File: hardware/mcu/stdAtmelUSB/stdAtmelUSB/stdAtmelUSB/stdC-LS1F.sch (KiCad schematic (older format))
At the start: 1 part

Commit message: std boards skeletons
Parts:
- added C2: 4.7uF, Capacitor_SMD:C_0402_1005Metric, symbol Device:C
- added C4: 0.1uF, Capacitor_SMD:C_0402_1005Metric, symbol Device:C
- J1: renamed from J?; footprint (none) -> Connector_PinHeader_2.54mm:PinHeader_1x20_P2.54mm_Horizontal
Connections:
- net labels added: fpga_cdone, fpga_reset, nrf_rx, nrf_tx, spi_clk, spi_miso, spi_mosi, spi_ss, uart_fpga_rx_2, uart_fpga_tx_2, uart_rx, uart_tx
- wire segments 2 -> 24
- no-connect marks 0 -> 1
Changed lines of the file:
@@
 $EndDescr
 $Comp
-L Connector:Conn_01x20_Female J?
+L Connector:Conn_01x20_Female J1
 U 1 1 5E9E9075
 P 2050 3500
-F 0 "J?" H 1942 2275 50  0000 C CNN
+F 0 "J1" H 1942 2275 50  0000 C CNN
 F 1 "Conn_01x20_Female" H 1942 2366 50  0000 C CNN
-F 2 "" H 2050 3500 50  0001 C CNN
+F 2 "Connector_PinHeader_2.54mm:PinHeader_1x20_P2.54mm_Horizontal" H 2050 3500 50  0001 C CNN
 F 3 "~" H 2050 3500 50  0001 C CNN
 	1    2050 3500
@@
 P 3350 1800
 AR Path="/5E9E6BE4/5E9ECCA0" Ref="#PWR?"  Part="1"
-AR Path="/5E9E8D09/5E9ECCA0" Ref="#PWR?"  Part="1"
-F 0 "#PWR?" H 3350 1650 50  0001 C CNN
+AR Path="/5E9E8D09/5E9ECCA0" Ref="#PWR04"  Part="1"
+F 0 "#PWR04" H 3350 1650 50  0001 C CNN
 F 1 "+3V3" H 3365 1973 50  0000 C CNN
 F 2 "" H 3350 1800 50  0001 C CNN
@@
 	1    0    0    -1
 $EndComp
-Wire Wire Line
-	3350 1800 3350 2050
 $Comp
-L power:GND #PWR?
+L power:GND #PWR03
 U 1 1 5E9EE351
 P 3000 4900
-F 0 "#PWR?" H 3000 4650 50  0001 C CNN
+F 0 "#PWR03" H 3000 4650 50  0001 C CNN
 F 1 "GND" H 3005 4727 50  0000 C CNN
 F 2 "" H 3000 4900 50  0001 C CNN
@@
 	1    0    0    -1
 $EndComp
+Text GLabel 2250 2900 2    50   Input ~ 0
+uart_tx
+Text GLabel 2250 2800 2    50   Input ~ 0
+uart_rx
+Text GLabel 2250 3300 2    50   Input ~ 0
+spi_clk
+Text GLabel 2250 3400 2    50   Input ~ 0
+spi_ss
+Text GLabel 2250 3500 2    50   Input ~ 0
+spi_miso
+Text GLabel 2250 3600 2    50   Input ~ 0
+spi_mosi
+Text GLabel 2250 3200 2    50   Input ~ 0
+fpga_reset
+Text GLabel 2250 3100 2    50   Input ~ 0
+fpga_cdone
+Text GLabel 2250 3800 2    50   Input ~ 0
+uart_fpga_tx_2
+Text GLabel 2250 3900 2    50   Input ~ 0
+uart_fpga_rx_2
+Text GLabel 2250 4200 2    50   Input ~ 0
+nrf_rx
+Text GLabel 2250 4300 2    50   Input ~ 0
+nrf_tx
+$Comp
+L Device:C C?
+U 1 1 5E9F19A3
+P 4600 2700
+AR Path="/5E9E6BB8/5E9F19A3" Ref="C?"  Part="1"
+AR Path="/5E9E8D09/5E9F19A3" Ref="C4"  Part="1"
+F 0 "C4" H 4715 2746 50  0000 L CNN
+F 1 "0.1uF" H 4715 2655 50  0000 L CNN
+F 2 "Capacitor_SMD:C_0402_1005Metric" H 4638 2550 50  0001 C CNN
+F 3 "~" H 4600 2700 50  0001 C CNN
+	1    4600 2700
+	1    0    0    -1
+$EndComp
+$Comp
+L Device:C C?
+U 1 1 5E9F19A9
+P 4050 2700
+AR Path="/5E9E6BB8/5E9F19A9" Ref="C?"  Part="1"
+AR Path="/5E9E8D09/5E9F19A9" Ref="C2"  Part="1"
+F 0 "C2" H 4165 2746 50  0000 L CNN
+F 1 "4.7uF" H 4165 2655 50  0000 L CNN
+F 2 "Capacitor_SMD:C_0402_1005Metric" H 4088 2550 50  0001 C CNN
+F 3 "~" H 4050 2700 50  0001 C CNN
+	1    4050 2700
+	1    0    0    -1
+$EndComp
+$Comp
+L power:GND #PWR?
+U 1 1 5E9F19AF
+P 4350 3350
+AR Path="/5E9E6BB8/5E9F19AF" Ref="#PWR?"  Part="1"
+AR Path="/5E9E8D09/5E9F19AF" Ref="#PWR06"  Part="1"
+F 0 "#PWR06" H 4350 3100 50  0001 C CNN
+F 1 "GND" H 4355 3177 50  0000 C CNN
+F 2 "" H 4350 3350 50  0001 C CNN
+F 3 "" H 4350 3350 50  0001 C CNN
+	1    4350 3350
+	1    0    0    -1
+$EndComp
+$Comp
+L power:+3V3 #PWR?
+U 1 1 5E9F19B5
+P 4350 2250
+AR Path="/5E9E6BB8/5E9F19B5" Ref="#PWR?"  Part="1"
+AR Path="/5E9E8D09/5E9F19B5" Ref="#PWR05"  Part="1"
+F 0 "#PWR05" H 4350 2100 50  0001 C CNN
+F 1 "+3V3" H 4365 2423 50  0000 C CNN
+F 2 "" H 4350 2250 50  0001 C CNN
+F 3 "" H 4350 2250 50  0001 C CNN
+	1    4350 2250
+	1    0    0    -1
+$EndComp
 Wire Wire Line
-	3000 4900 3000 4700
+	4050 2850 4050 3150
+Wire Wire Line
+	4050 3150 4350 3150
+Wire Wire Line
+	4600 3150 4600 2850
+Wire Wire Line
+	4050 2550 4050 2400
+Wire Wire Line
+	4050 2400 4350 2400
+Wire Wire Line
+	4600 2400 4600 2550
+Wire Wire Line
+	4350 2250 4350 2400
+Connection ~ 4350 2400
+Wire Wire Line
+	4350 2400 4600 2400
+Wire Wire Line
+	4350 3350 4350 3150
+Connection ~ 4350 3150
+Wire Wire Line
+	4350 3150 4600 3150
+Wire Wire Line
+	2250 2500 3000 2500
+Wire Wire Line
+	3000 2500 3000 2700
+Wire Wire Line
+	2250 2600 3350 2600
+Wire Wire Line
+	3350 1800 3350 2600
+Connection ~ 3000 2700
+Wire Wire Line
+	3000 2700 3000 3000
+Wire Wire Line
+	2250 2700 3000 2700
+Wire Wire Line
+	2250 4400 3000 4400
+Connection ~ 3000 4400
+Wire Wire Line
+	3000 4400 3000 4900
+Wire Wire Line
+	2250 4100 3000 4100
+Connection ~ 3000 4100
+Wire Wire Line
+	3000 4100 3000 4400
+Wire Wire Line
+	2250 3700 3000 3700
+Connection ~ 3000 3700
+Wire Wire Line
+	3000 3700 3000 4100
+NoConn ~ 2250 4000
+Wire Wire Line
+	2250 3000 3000 3000
+Connection ~ 3000 3000
+Wire Wire Line
+	3000 3000 3000 3700
 $EndSCHEMATC

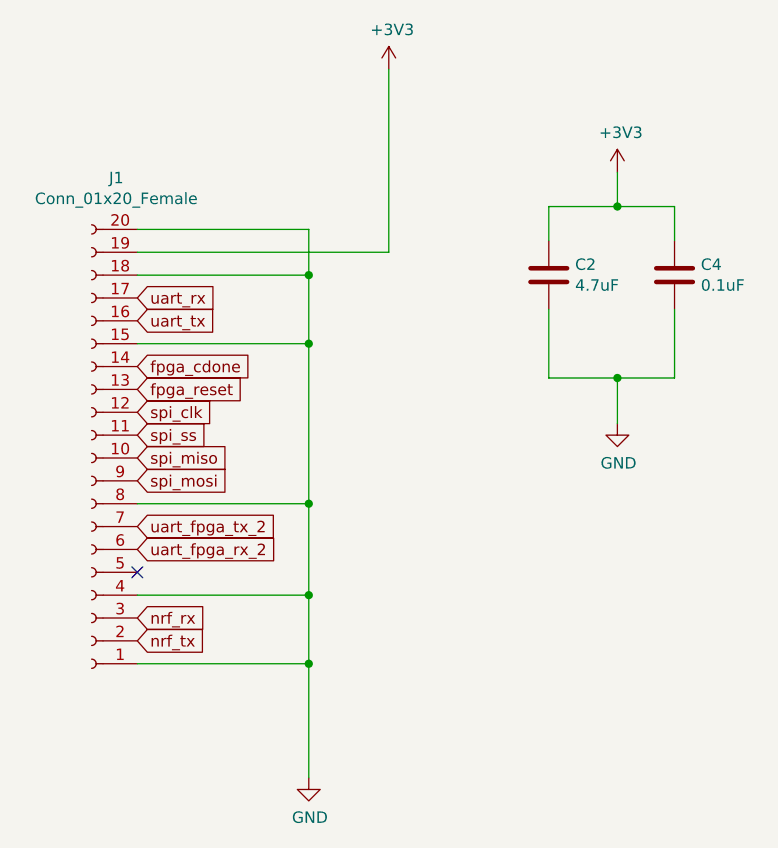
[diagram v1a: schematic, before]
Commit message: u-blox GPS CAM-M8Q
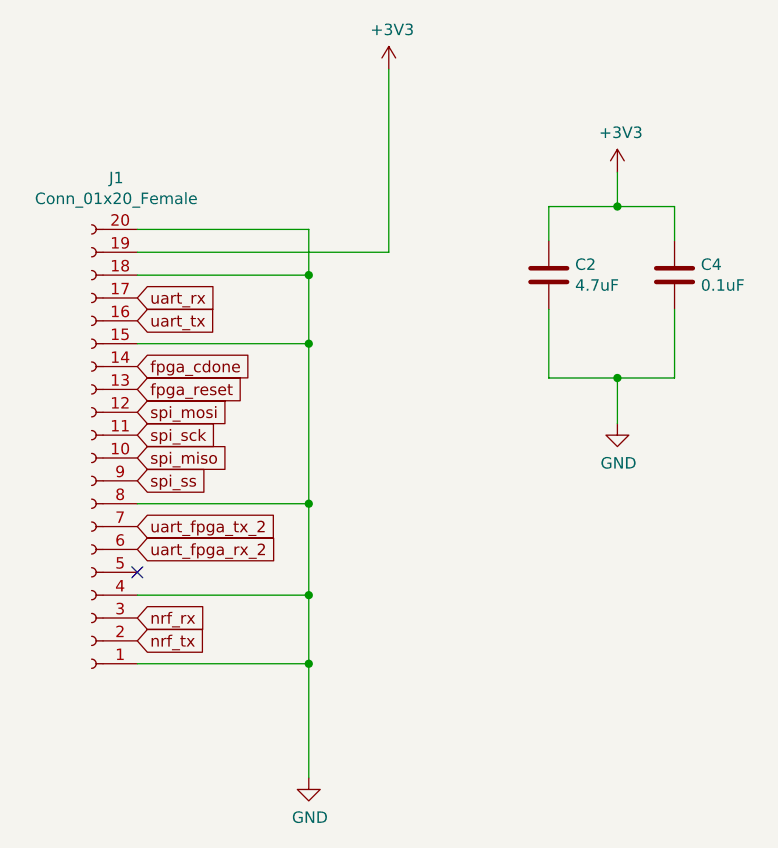
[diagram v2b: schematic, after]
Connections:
- net spi_clk is gone; now on net spi_mosi: J1.12 (Pin_12)
- net spi_mosi: no longer J1.9 (Pin_9)
- net spi_ss: now also J1.9 (Pin_9); no longer J1.11 (Pin_11)
- new net spi_sck: J1.11 (Pin_11)
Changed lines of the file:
@@
 uart_rx
 Text GLabel 2250 3300 2    50   Input ~ 0
-spi_clk
+spi_mosi
 Text GLabel 2250 3400 2    50   Input ~ 0
-spi_ss
+spi_sck
 Text GLabel 2250 3500 2    50   Input ~ 0
 spi_miso
 Text GLabel 2250 3600 2    50   Input ~ 0
-spi_mosi
+spi_ss
 Text GLabel 2250 3200 2    50   Input ~ 0
 fpga_reset
